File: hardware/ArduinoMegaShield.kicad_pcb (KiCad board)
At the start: 2 copper layers, 40 parts, among them J201 DB15, J202 DB9, J203 DB9, P201 CONN_01X02, P202 CONN_01X08, P203 CONN_01X08, SW101 SW_Coded, SW102 SW_Coded, SW103 SW_Coded, U101 A4988, U102 A4988, U103 A4988

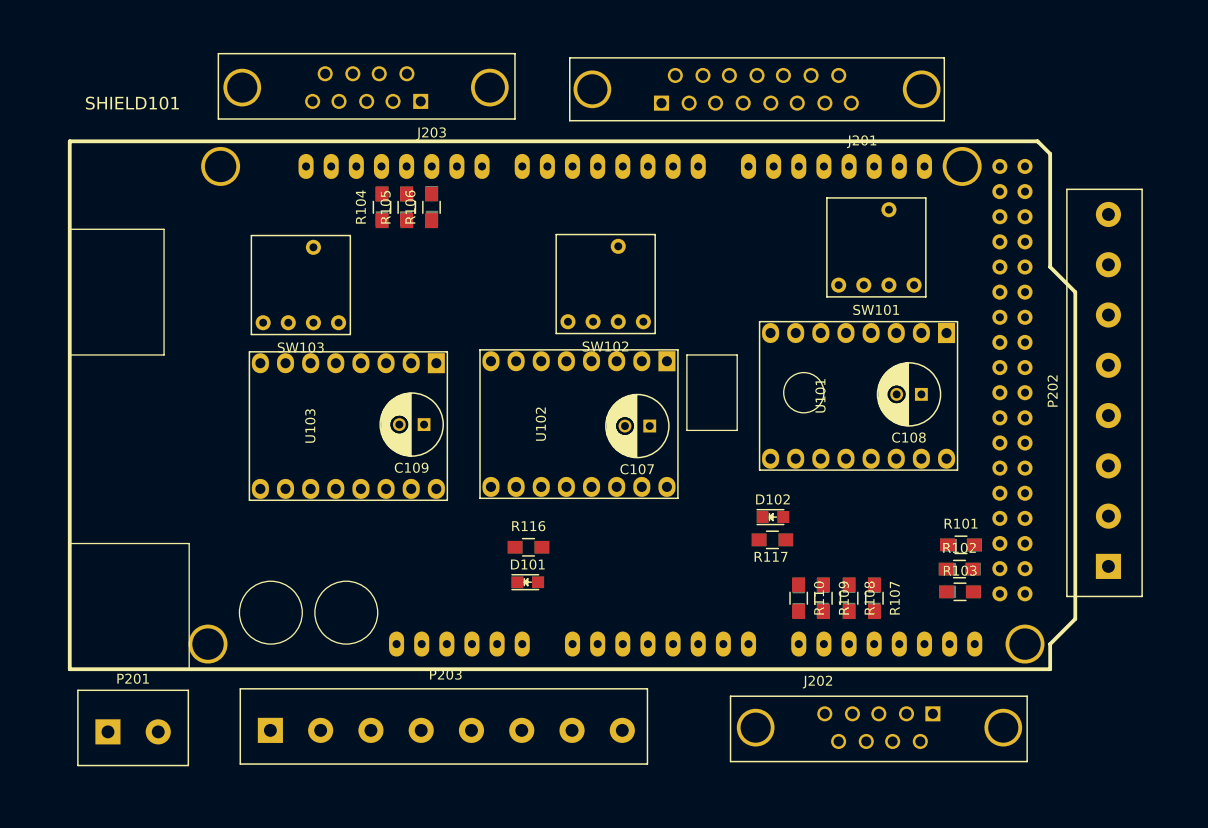
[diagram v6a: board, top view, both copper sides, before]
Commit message: changed dsub connectors to horizontal
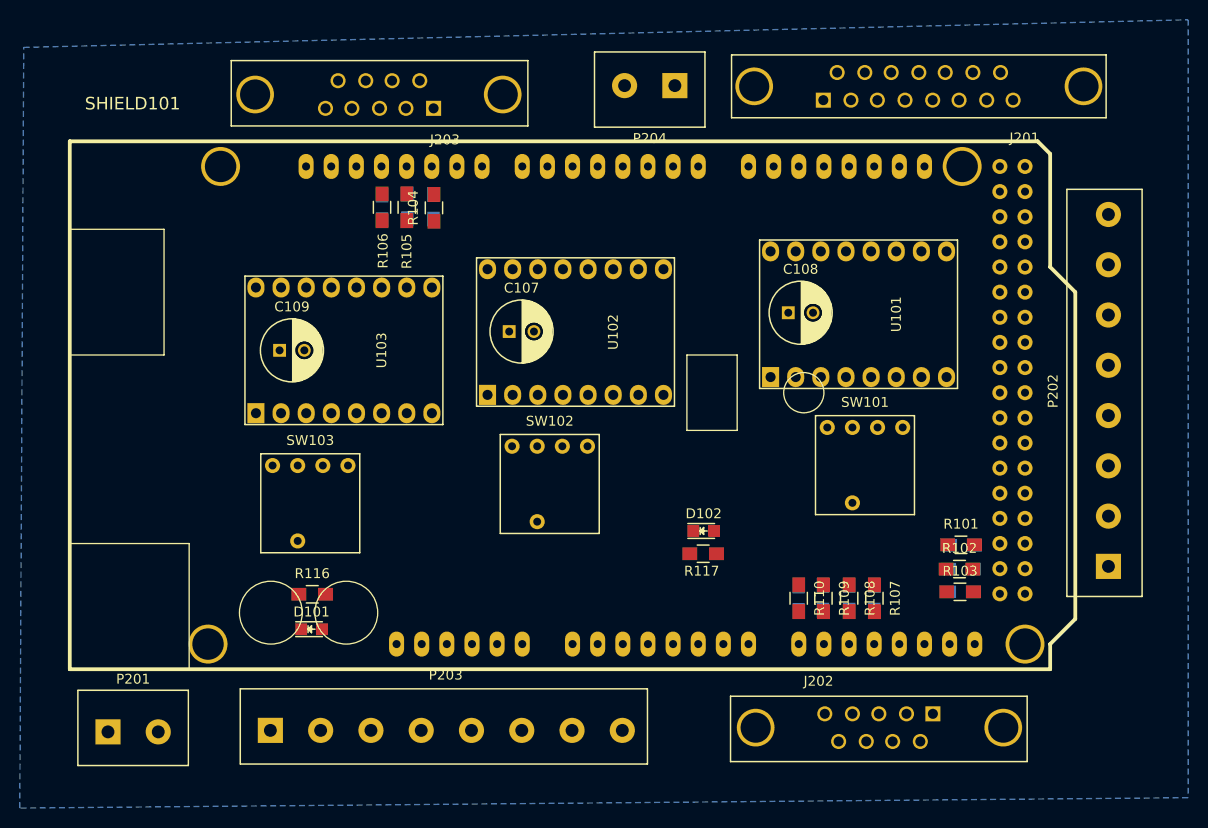
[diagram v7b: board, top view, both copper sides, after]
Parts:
- added P204: CONN_01X02, 6axis:Terminal_Block_200_mil, F.Cu at (132.6, 75.0)
- moved D101 22.4 mm to (98.4, 129.9)
- moved R116 22.4 mm to (98.5, 126.3)
- moved SW103 22.1 mm to (98.2, 117.2), turned to 180 degrees
- moved SW101 22.0 mm to (154.3, 113.3), turned to 180 degrees
- moved SW102 21.0 mm to (122.5, 115.2), turned to 180 degrees
- moved C107 17.1 mm to (118.3, 99.8), turned to 0 degrees
- moved C109 16.4 mm to (95.2, 101.7), turned to 0 degrees
- moved J201 16.4 mm to (160.2, 75.2)
- moved C108 15.8 mm to (146.6, 97.9), turned to 0 degrees
- moved U102 9.31 mm to (125.0, 99.8), turned to 90 degrees
- moved U101 8.25 mm to (153.7, 98.0), turned to 90 degrees
- moved U103 7.66 mm to (101.7, 101.7), turned to 90 degrees
- moved D102 7.14 mm to (138.0, 120.0)
- moved R117 7.14 mm to (137.9, 122.2)
- moved R104 5.25 mm to (110.8, 87.3)
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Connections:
- J203 pad 1: /X_LIMIT -> GND
- P202 pad 2: /~X-Step -> /~Z-Dir
- P202 pad 3: /~X-Dir -> /~Y-Dir
- P202 pad 4: /~Y-Step -> /~X-Dir
- P202 pad 5: /~Y-Dir -> /~Z-Step
- P202 pad 6: /~Z-Step -> /~Y-Step
- P202 pad 7: /~Z-Dir -> /~X-Step
- P203 pad 1: /CYCLE_START -> /RESET
- P203 pad 5: /SAFETY_DOOR -> /CYCLE_START
- P203 pad 7: /RESET -> /SAFETY_DOOR
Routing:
- added copper zone on B.Cu, net GND
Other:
- net class Default: clearance 0.2 -> 0.1524; trace_width 0.25 -> 0.2032; via_dia 0.6 -> 0.6858; via_drill 0.4 -> 0.3302
- rule trace_clearance: 0.2 -> 0.1524
- rule trace_min: 0.2 -> 0.1524
- rule via_min_drill: 0.3 -> 0.3302
- rule via_min_size: 0.4 -> 0.6858

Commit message: completed board and generated gerbers
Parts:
- J201: footprint Connectors:DB15FD -> 6axis:D15S33E4GV00LF
- J202: footprint Connectors:DB9FD -> 6axis:LD09S33E4GV00LF
- J203: footprint Connectors:DB9MD -> 6axis:LD09P33E4GV00LF
- moved D102 59.3 mm to (87.1, 89.4), turned to 180 degrees
- moved R117 59.0 mm to (87.1, 92.2), turned to 180 degrees
- moved P204 5.07 mm to (131.1, 70.1)
- moved P201 5.04 mm to (82.5, 144.8)
- moved P203 4.05 mm to (113.0, 144.0)
- moved J202 1.52 mm to (154.7, 138.8), turned to 180 degrees
- moved J201 1.48 mm to (159.0, 75.9), turned to 0 degrees
- moved J203 1.43 mm to (106.7, 75.9), turned to 0 degrees
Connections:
- J201 pad 1: /C2B -> /C1A
- J201 pad 10: /C1A -> /C2A
- J201 pad 11: /B2A -> /B2B
- J201 pad 12: /B1B -> /B1A
- J201 pad 14: /A2A -> /A2B
- J201 pad 15: /A1B -> /A1A
- J201 pad 3: /B2B -> /B2A
- J201 pad 4: GND -> /B1B
- J201 pad 5: /B1A -> GND
- J201 pad 6: /A2B -> /A2A
- J201 pad 7: GND -> /A1B
- J201 pad 8: /A1A -> GND
- J201 pad 9: /C2A -> /C2B
- P202 pad 3: /~Y-Dir -> /~X-Dir
- P202 pad 4: /~X-Dir -> /~Y-Dir
- P202 pad 6: /~Y-Step -> /~X-Step
- P202 pad 7: /~X-Step -> /~Y-Step
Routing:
- net +5V: track 0.00 -> 368.0 mm, vias 0 -> 4
- net /~ENABLE: track 0.00 -> 165.5 mm, vias 0 -> 2
- net +12V: track 0.00 -> 132.2 mm
- net /C-Step: track 0.00 -> 69.8 mm, vias 0 -> 2
- net /C2B: track 0.00 -> 67.6 mm
- net /C2A: track 0.00 -> 67.2 mm
- net /RESET: track 0.00 -> 65.3 mm
- net /C-Dir: track 0.00 -> 64.0 mm, vias 0 -> 1
- net /FEED_HOLD: track 0.00 -> 58.9 mm
- net /C_LIMIT: track 0.00 -> 55.9 mm, vias 0 -> 1
- net /C1B: track 0.00 -> 55.6 mm
- net /C1A: track 0.00 -> 55.4 mm
- net /CYCLE_START: track 0.00 -> 50.4 mm
- net /B2B: track 0.00 -> 46.2 mm
- net /B1A: track 0.00 -> 44.5 mm
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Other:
- board outline added: 109.2 x 81.8 mm
- net class Default: clearance 0.1524 -> 0.2032
- rule trace_clearance: 0.1524 -> 0.2032
- board text added: "+12V"
- board text added: "6-Axis Robot Arm Control Shield Designed By: Alan Ford David Andra Bruce Davies"
- board text added: "CYCL_START"
- board text added: "FD_HOLD"
- board text added: "GND"
- board text added: "RESET"
- board text added: "SFTY_DR"
- board text added: "X_LMT"
